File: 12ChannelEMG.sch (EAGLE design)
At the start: 243 parts

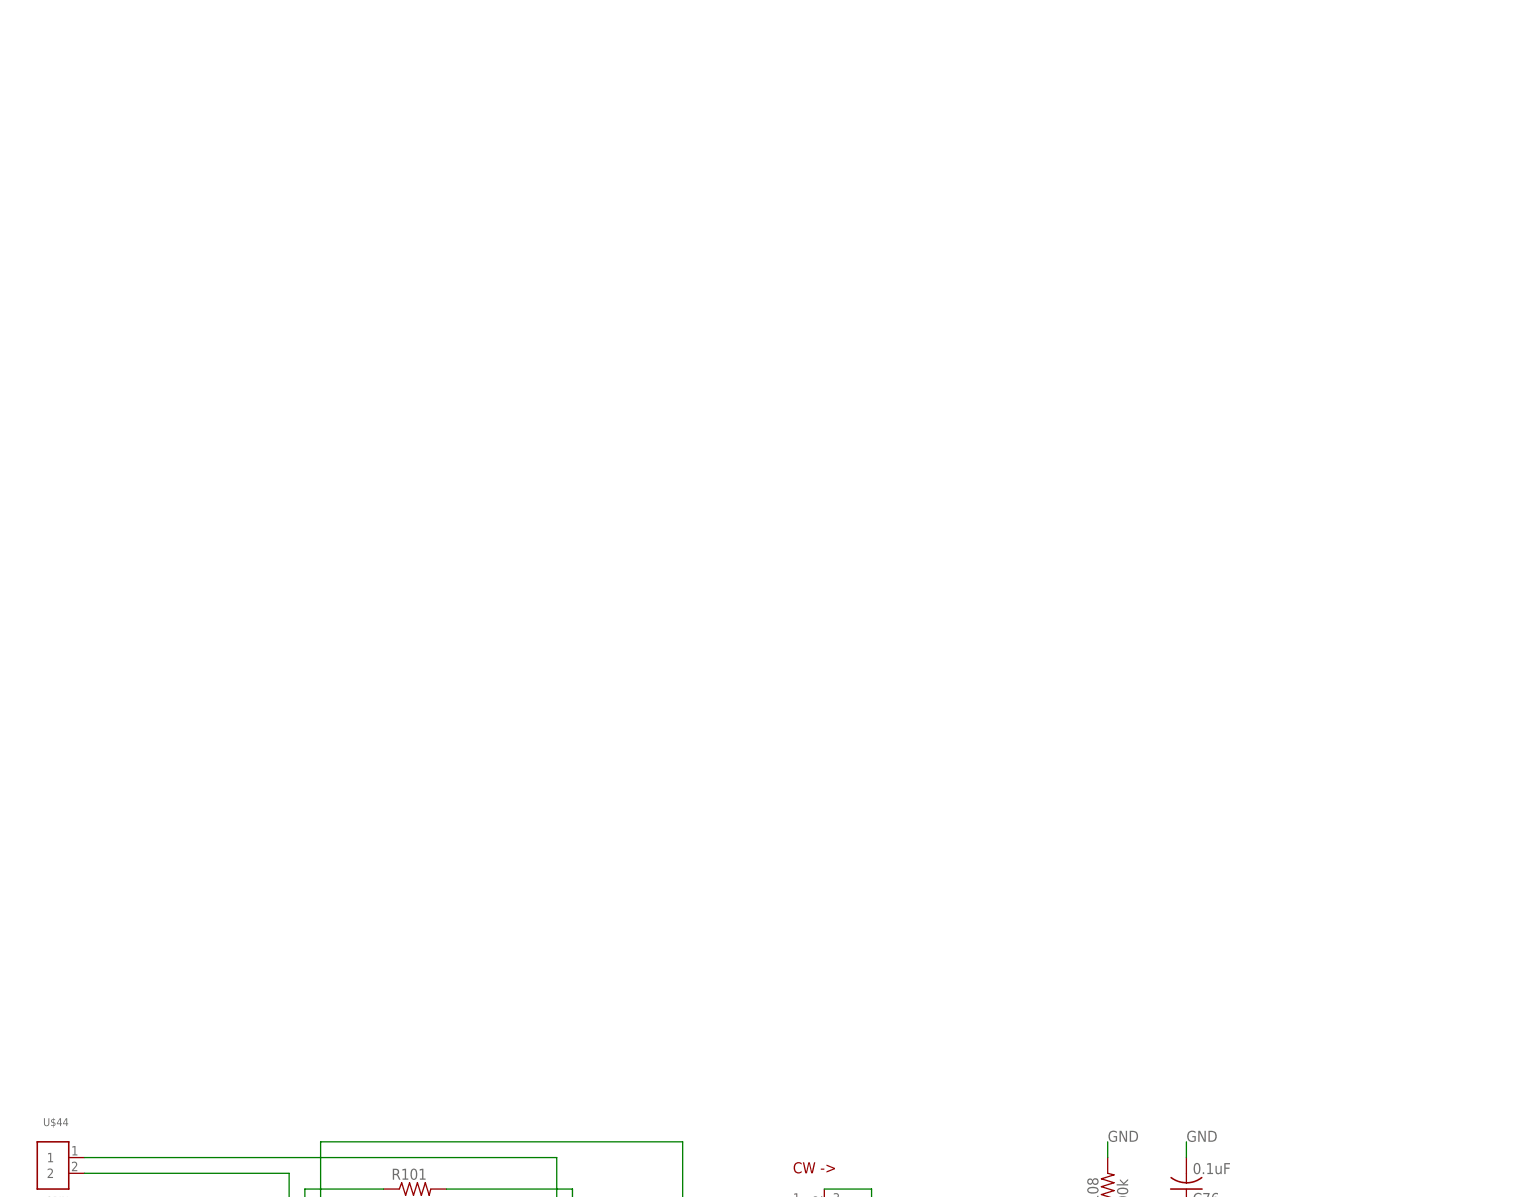
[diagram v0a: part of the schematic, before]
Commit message: Channel 14, all channels done
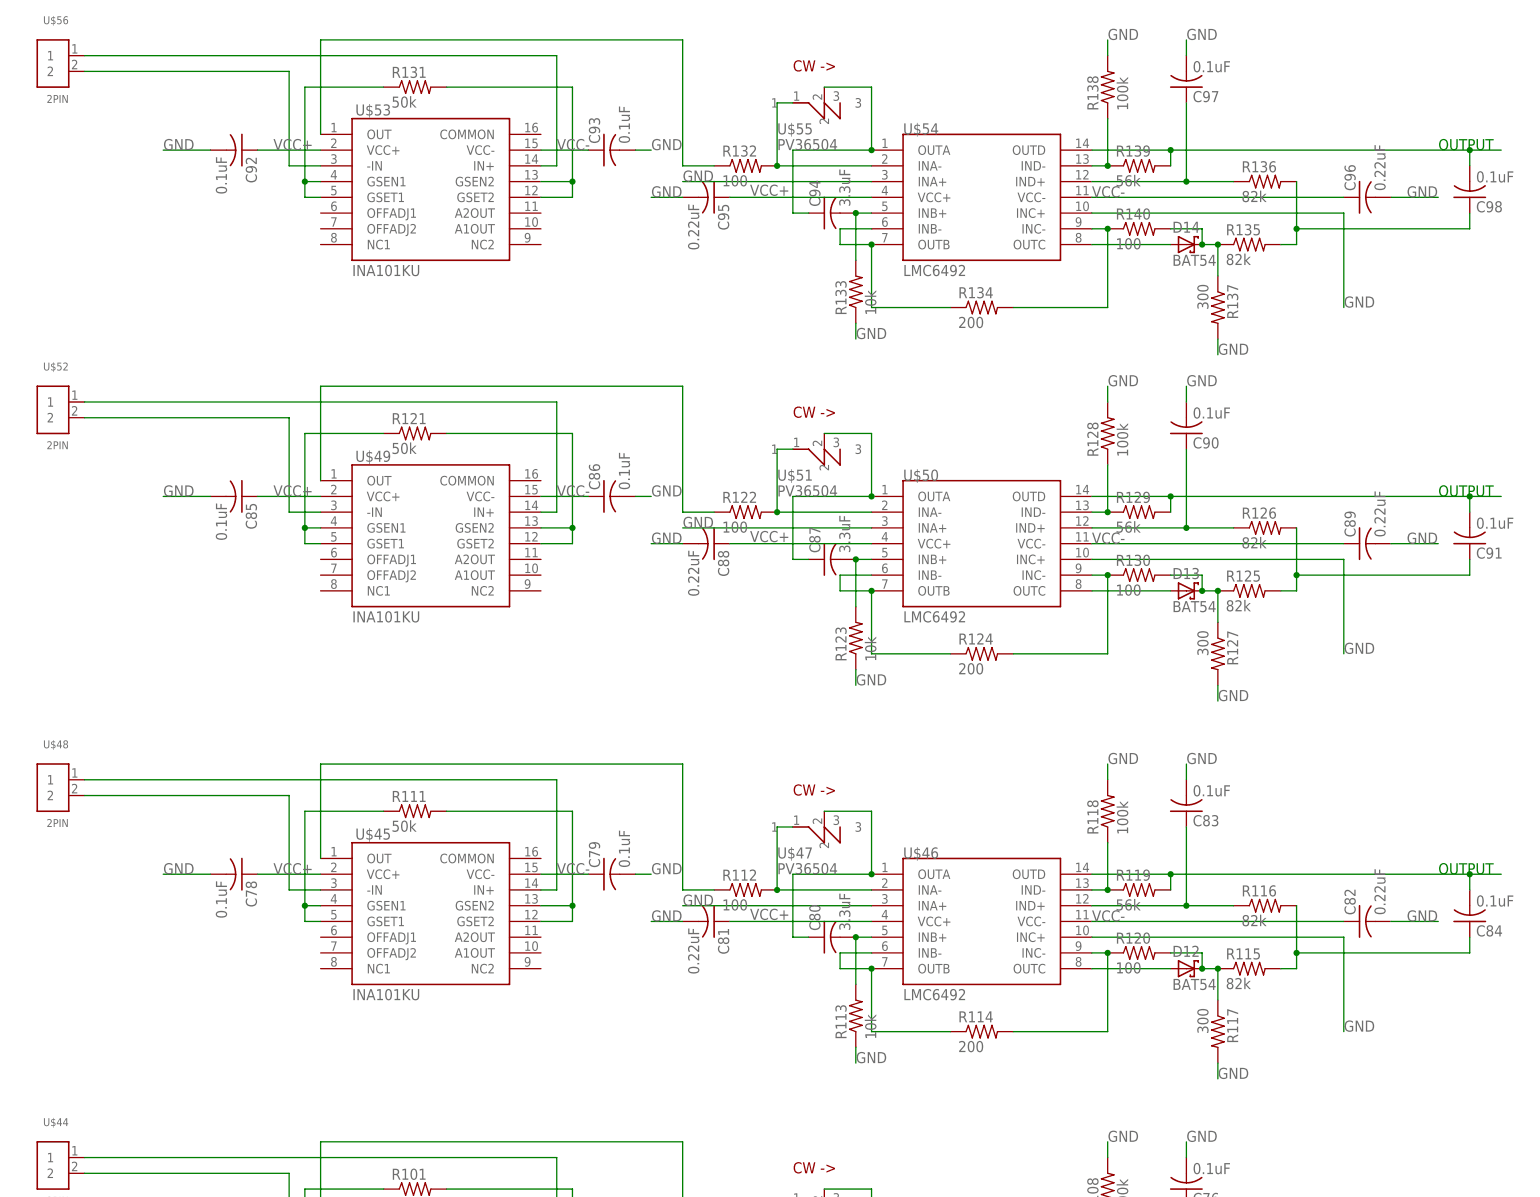
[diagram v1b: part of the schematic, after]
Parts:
- added C78, C79, C83, C84, C85, C86, C90, C91, C92, C93, C97, C98: 0.1uF, resistor:C-USC1206K
- added C80, C87, C94: 3.3uF, resistor:C-USC1206K
- added C81, C82, C88, C89, C95, C96: 0.22uF, rcl:C-USC0603K
- added D12, D13, D14: BAT54, diode:BAT54
- added R111, R121, R131: 50k, rcl:R-US_R0805
- added R112, R120, R122, R130, R132, R140: 100, resistor:R-US_R0603
- added R113, R123, R133: 10k, rcl:R-US_R0603
- added R114, R124, R134: 200, rcl:R-US_R0603
- added R115, R116, R125, R126, R135, R136: 82k, resistor:R-US_R0603
- added R117, R127, R137: 300, resistor:R-US_R0603
- added R118, R128, R138: 100k, resistor:R-US_R0603
- added R119, R129, R139: 56k, resistor:R-US_R0603
- added U$45, U$49, U$53: INA101KU, 12-ChannelEMG:INA101KUINA101KU
- added U$46, U$50, U$54: LMC6492, 12-ChannelEMG:LMC6492
- added U$47, U$51, U$55: PV36504, 12-ChannelEMG:PV36
- added U$48, U$52, U$56: 2PIN, 12-ChannelEMG:2PIN
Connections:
- new net N$179: R111.2, U$45.GSEN2, U$45.GSET2
- new net N$180: U$45.-IN, U$48.2
- new net N$181: R112.2, U$46.INA-, U$47.1
- new net N$182: R112.1, U$45.OUT
- new net N$183: C80.1, U$46.OUTA, U$47.2
- new net N$184: C80.2, R113.2, U$46.INB+
- new net N$185: R114.1, U$46.INB-, U$46.OUTB
- new net N$186: R114.2, R120.1, U$46.INC-
- new net N$187: D12.A, U$46.OUTC
- new net N$188: C83.1, R116.1, U$46.IND+
- new net N$189: D12.C, R115.1, R117.1, R120.2
- new net N$190: C84.2, R119.2, U$46.OUTD
- new net N$191: R118.1, R119.1, U$46.IND-
- new net N$192: C84.1, R115.2, R116.2
- new net N$193: R111.1, U$45.GSEN1, U$45.GSET1
- new net N$194: U$45.IN+, U$48.1
- new net N$195: R121.2, U$49.GSEN2, U$49.GSET2
- new net N$196: U$49.-IN, U$52.2
- new net N$197: R122.2, U$50.INA-, U$51.1
- new net N$198: R122.1, U$49.OUT
- new net N$199: C87.1, U$50.OUTA, U$51.2
- new net N$200: C87.2, R123.2, U$50.INB+
- new net N$201: R124.1, U$50.INB-, U$50.OUTB
- new net N$202: R124.2, R130.1, U$50.INC-
- new net N$203: D13.A, U$50.OUTC
- new net N$204: C90.1, R126.1, U$50.IND+
- new net N$205: D13.C, R125.1, R127.1, R130.2
- new net N$206: C91.2, R129.2, U$50.OUTD
- new net N$207: R128.1, R129.1, U$50.IND-
- new net N$208: C91.1, R125.2, R126.2
- new net N$209: R121.1, U$49.GSEN1, U$49.GSET1
- new net N$210: U$49.IN+, U$52.1
- new net N$211: R131.2, U$53.GSEN2, U$53.GSET2
- new net N$212: U$53.-IN, U$56.2
- new net N$213: R132.2, U$54.INA-, U$55.1
- new net N$214: R132.1, U$53.OUT
- new net N$215: C94.1, U$54.OUTA, U$55.2
- new net N$216: C94.2, R133.2, U$54.INB+
- new net N$217: R134.1, U$54.INB-, U$54.OUTB
- new net N$218: R134.2, R140.1, U$54.INC-
- new net N$219: D14.A, U$54.OUTC
- new net N$220: C97.1, R136.1, U$54.IND+
- new net N$221: D14.C, R135.1, R137.1, R140.2
- new net N$222: C98.2, R139.2, U$54.OUTD
- new net N$223: R138.1, R139.1, U$54.IND-
- new net N$224: C98.1, R135.2, R136.2
- new net N$225: R131.1, U$53.GSEN1, U$53.GSET1
- new net N$226: U$53.IN+, U$56.1
- net GND: now also C78.2, C79.2, C81.2, C82.2, C83.2, C85.2, C86.2, C88.2, C89.2, C90.2, C92.2, C93.2, C95.2, C96.2, C97.2, R113.1, R117.2, R118.2, R123.1, R127.2, R128.2, R133.1, R137.2, R138.2, U$46.INA+, U$46.INC+, U$50.INA+, U$50.INC+, U$54.INA+, U$54.INC+
- net VCC+: now also C78.1, C81.1, C85.1, C88.1, C92.1, C95.1, U$45.VCC+, U$46.VCC+, U$49.VCC+, U$50.VCC+, U$53.VCC+, U$54.VCC+
- net VCC-: now also C79.1, C82.1, C86.1, C89.1, C93.1, C96.1, U$45.VCC-, U$46.VCC-, U$49.VCC-, U$50.VCC-, U$53.VCC-, U$54.VCC-

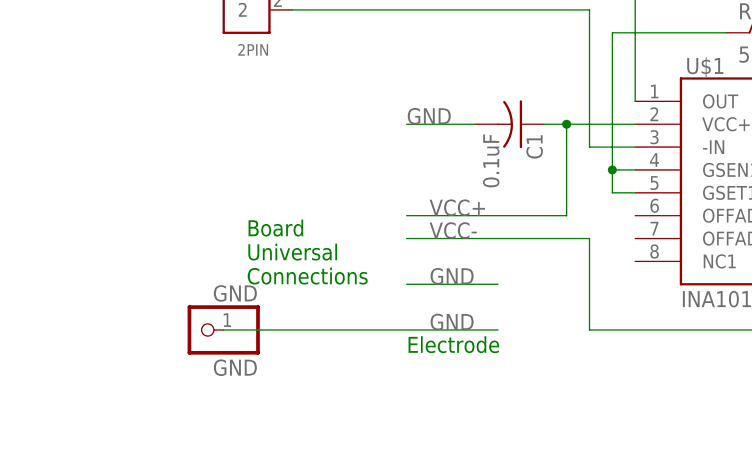
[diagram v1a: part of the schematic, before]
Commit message: Added power connector
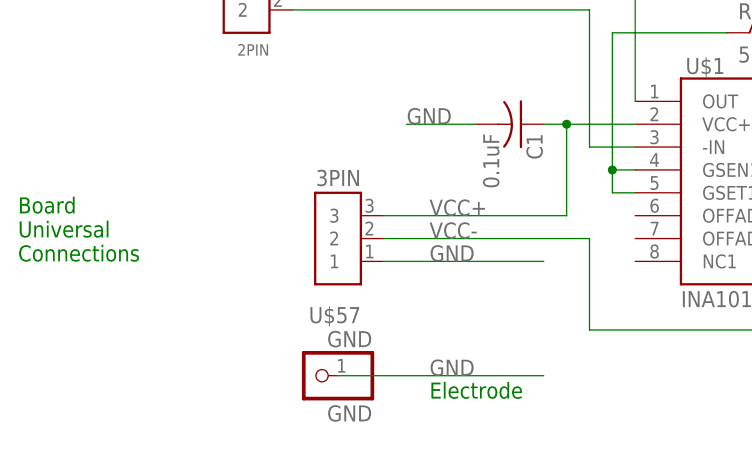
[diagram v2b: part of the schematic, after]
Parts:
- added U$57: 3PIN, 12-ChannelEMG:3PIN
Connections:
- net GND: now also U$57.1
- net VCC+: now also U$57.3
- net VCC-: now also U$57.2
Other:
- moved on the sheet: GND
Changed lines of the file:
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@@
 <part name="R140" library="resistor" deviceset="R-US_" device="R0603" value="100"/>
 <part name="U$56" library="12-ChannelEMG" deviceset="2PIN" device=""/>
+<part name="U$57" library="12-ChannelEMG" deviceset="3PIN" device=""/>
 </parts>
 <sheets>
 <sheet>
 <plain>
-<text x="-17.78" y="22.86" size="1.778" layer="91">Electrode</text>
-<text x="-35.56" y="30.48" size="1.778" layer="91">Board
+<text x="-15.24" y="17.78" size="1.778" layer="91">Electrode</text>
+<text x="-60.96" y="33.02" size="1.778" layer="91">Board
 Universal
 Connections</text>
@@
 <instance part="R9" gate="G$1" x="139.7" y="45.72"/>
 <instance part="R10" gate="G$1" x="139.7" y="35.56"/>
-<instance part="GND" gate="G$1" x="-40.64" y="25.4" rot="MR0"/>
+<instance part="GND" gate="G$1" x="-27.94" y="20.32" rot="MR0"/>
 <instance part="U$10" gate="G$1" x="-35.56" y="63.5" rot="MR0"/>
 <instance part="U$4" gate="G$1" x="25.4" y="104.14"/>
@@
 <instance part="R140" gate="G$1" x="139.7" y="797.56"/>
 <instance part="U$56" gate="G$1" x="-35.56" y="825.5" rot="MR0"/>
+<instance part="U$57" gate="G$1" x="-25.4" y="35.56" rot="R180"/>
 </instances>
 <busses>
@@
 <wire x1="0" y1="48.26" x2="-2.54" y2="48.26" width="0.1524" layer="91"/>
 <wire x1="0" y1="48.26" x2="0" y2="38.1" width="0.1524" layer="91"/>
-<wire x1="0" y1="38.1" x2="-17.78" y2="38.1" width="0.1524" layer="91"/>
+<wire x1="0" y1="38.1" x2="-20.32" y2="38.1" width="0.1524" layer="91"/>
 <label x="-15.24" y="38.1" size="1.778" layer="95"/>
 <junction x="0" y="48.26"/>
+<pinref part="U$57" gate="G$1" pin="3"/>
 </segment>
 <segment>
@@
 <wire x1="50.8" y1="25.4" x2="2.54" y2="25.4" width="0.1524" layer="91"/>
 <wire x1="2.54" y1="25.4" x2="2.54" y2="35.56" width="0.1524" layer="91"/>
-<wire x1="2.54" y1="35.56" x2="-17.78" y2="35.56" width="0.1524" layer="91"/>
+<wire x1="2.54" y1="35.56" x2="-20.32" y2="35.56" width="0.1524" layer="91"/>
 <label x="-15.24" y="35.56" size="1.778" layer="95"/>
 <junction x="50.8" y="48.26"/>
+<pinref part="U$57" gate="G$1" pin="2"/>
 </segment>
 <segment>
@@
 </segment>
 <segment>
-<wire x1="-17.78" y1="30.48" x2="-7.62" y2="30.48" width="0.1524" layer="91"/>
-<label x="-15.24" y="30.48" size="1.778" layer="95"/>
-<wire x1="-38.1" y1="25.4" x2="-7.62" y2="25.4" width="0.1524" layer="91"/>
-<label x="-15.24" y="25.4" size="1.778" layer="95"/>
+<wire x1="-20.32" y1="33.02" x2="-2.54" y2="33.02" width="0.1524" layer="91"/>
+<label x="-15.24" y="33.02" size="1.778" layer="95"/>
+<wire x1="-25.4" y1="20.32" x2="-2.54" y2="20.32" width="0.1524" layer="91"/>
+<label x="-15.24" y="20.32" size="1.778" layer="95"/>
 <pinref part="GND" gate="G$1" pin="1"/>
-</segment>
-<segment>
+<pinref part="U$57" gate="G$1" pin="1"/>
+</segment>
+<segment>

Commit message: Added 15 pin output
Board finished, need to add silk screen markings
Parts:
- added U$58: 15PIN, 12-ChannelEMG:15PIN
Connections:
- net GND: now also U$58.15
- net N$100: now also U$28.IN-; no longer U$28.2
- net N$110: now also U$58.8
- net N$114: now also U$28.IN+; no longer U$28.1
- net N$116: now also U$32.IN-; no longer U$32.2
- net N$126: now also U$58.7
- net N$130: now also U$32.IN+; no longer U$32.1
- net N$132: now also U$36.IN-; no longer U$36.2
- net N$14: now also U$58.14
- net N$142: now also U$58.6
- net N$146: now also U$36.IN+; no longer U$36.1
- net N$148: now also U$40.IN-; no longer U$40.2
- net N$158: now also U$58.5
- net N$162: now also U$40.IN+; no longer U$40.1
- net N$164: now also U$44.IN-; no longer U$44.2
- net N$174: now also U$58.4
- net N$178: now also U$44.IN+; no longer U$44.1
- net N$180: now also U$48.IN-; no longer U$48.2
- net N$190: now also U$58.3
- net N$194: now also U$48.IN+; no longer U$48.1
- net N$196: now also U$52.IN-; no longer U$52.2
- net N$20: now also U$7.IN-; no longer U$7.2
- net N$206: now also U$58.2
- net N$210: now also U$52.IN+; no longer U$52.1
- net N$212: now also U$56.IN-; no longer U$56.2
- net N$222: now also U$58.1
- net N$226: now also U$56.IN+; no longer U$56.1
- net N$30: now also U$58.13
- net N$34: now also U$7.IN+; no longer U$7.1
- net N$36: now also U$12.IN-; no longer U$12.2
- net N$46: now also U$58.12
- net N$50: now also U$12.IN+; no longer U$12.1
- net N$52: now also U$16.IN-; no longer U$16.2
- net N$6: now also U$10.IN-; no longer U$10.2
- net N$62: now also U$58.11
- net N$66: now also U$16.IN+; no longer U$16.1
- net N$68: now also U$20.IN-; no longer U$20.2
- net N$7: now also U$10.IN+; no longer U$10.1
- net N$78: now also U$58.10
- net N$82: now also U$20.IN+; no longer U$20.1
- net N$84: now also U$24.IN-; no longer U$24.2
- net N$94: now also U$58.9
- net N$98: now also U$24.IN+; no longer U$24.1
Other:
- moved on the sheet: U$10, U$12, U$16, U$20, U$24, U$28, U$32, U$36, U$40, U$44, U$48, U$52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
